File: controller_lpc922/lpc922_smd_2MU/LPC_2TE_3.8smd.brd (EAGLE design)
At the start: 30.5 x 58.1 mm, 46 parts, among them IC1 MC34063AD, Q1 BC856, Q2 BC847C, Q3 BCP52

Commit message: Type of LDO added (VALUE in Schematic and Board added).
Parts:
- IC3: value (none) -> MCP1702-3302
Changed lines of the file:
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@@
 <attribute name="VALUE" x="23.9713" y="33.3376" size="1.27" layer="27" rot="R90"/>
 </element>
-<element name="IC3" library="v-reg" package="79LXX" value="" x="4.1275" y="4.1275" smashed="yes">
+<element name="IC3" library="v-reg" package="79LXX" value="MCP1702-3302" x="4.1275" y="4.1275" smashed="yes">
 <attribute name="NAME" x="3.3337" y="7.1438" size="0.8128" layer="25" ratio="10"/>
-<attribute name="VALUE" x="7.3025" y="2.8575" size="1.27" layer="27" ratio="10"/>
+<attribute name="VALUE" x="7.3025" y="2.8575" size="1.27" layer="27" ratio="10" display="off"/>
 </element>
 <element name="C7" library="rcl" package="E2-5" value="1µ" x="17.4626" y="9.3663" smashed="yes">

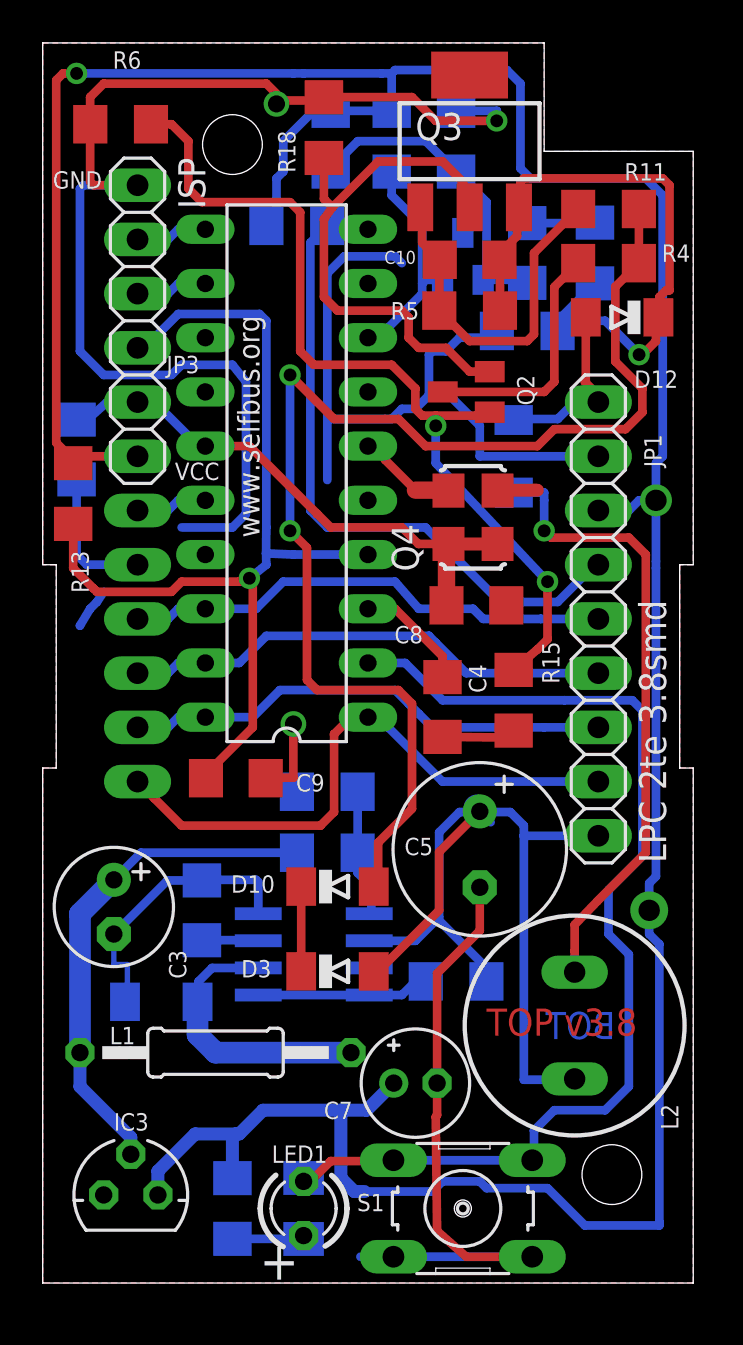
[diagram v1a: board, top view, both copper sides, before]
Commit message: 3D models added + some rework
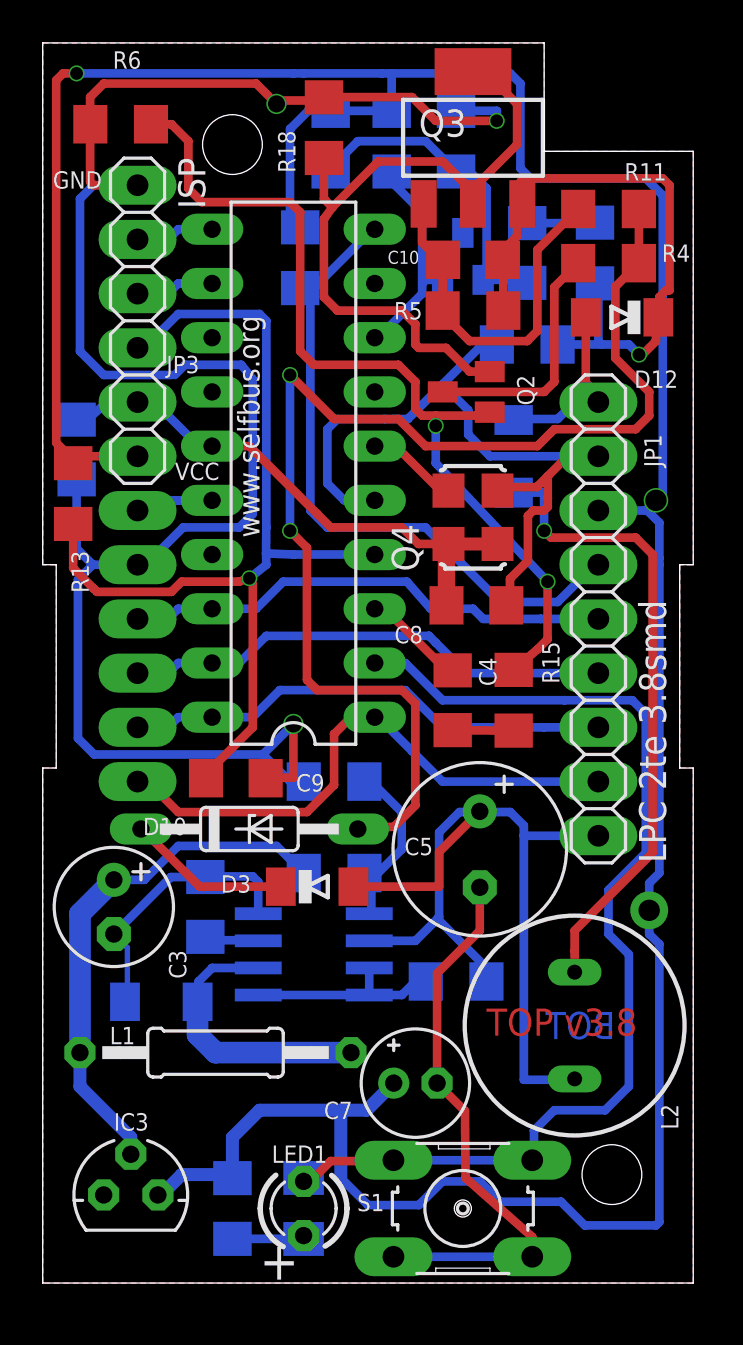
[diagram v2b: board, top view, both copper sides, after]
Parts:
- 89LPC922: device micro-philips:DIL20@1 -> MyIC-MCU:DIL20
- D10: device diode:MINIMELF -> diode:DO35Z10
- JP1: device pinhead:1X09 -> pinhead-1:1X09_LONG
- Q4: value (none) -> ASFL1
- moved D10 4.93 mm to (9.68, 21.3)
- moved D3 4.08 mm to (12.9, 18.6)
- moved R17 1.50 mm to (12.1, 48.0), turned to 270 degrees
- moved R2 1.00 mm to (13.7, 19.2)
- moved R3 0.64 mm to (22.7, 44.0)
- moved R10 0.57 mm to (13.7, 23.5)
- moved C4 0.57 mm to (19.2, 27.3)
- moved 89LPC922 0.32 mm to (11.7, 37.9)
- moved C6 0.22 mm to (7.62, 17.6)
- moved Q3 0.22 mm to (20.2, 53.7)
- moved C10 0.16 mm to (20.2, 47.9)
- moved R5 0.16 mm to (20.2, 45.6)
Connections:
- net I_SENSE: now also Q3.4
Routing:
- net GND: track 152.6 -> 169.9 mm
- net I_SENSE: track 25.2 -> 33.4 mm
- net N$15: track 3.97 -> 7.69 mm
- net VCC: track 155.2 -> 152.1 mm
- net EIB_DC: track 44.9 -> 42.4 mm
- net FEEDBACK: track 6.02 -> 8.37 mm
- net P0.0: track 27.9 -> 26.7 mm
- net PWM: track 32.8 -> 31.6 mm
- net PROG: track 51.3 -> 50.2 mm
- net N$4: track 30.3 -> 29.4 mm
- net VCC_5V: track 23.6 -> 24.6 mm
- net N$6: track 5.12 -> 4.32 mm
- net REFERENZ: track 58.4 -> 57.6 mm
- net P0.2: track 23.0 -> 23.7 mm
- net N$17: track 3.47 -> 2.86 mm
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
